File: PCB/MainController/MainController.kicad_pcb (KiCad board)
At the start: 2 copper layers, 124 x 48 mm, 58 parts, among them J1 5V, J10 Jack-DC, J11 MH, J12 MH, J2 PGM, J3 SERIAL, J4 I2C, J5 IO, J6 PWR, J7 MH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

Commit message: opening mplab
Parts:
- added J13: PIC_IO, Pin_Headers:Pin_Header_Straight_1x05_Pitch2.54mm, F.Cu at (131.0, 62.5)
- moved D5 5.41 mm to (139.0, 71.5)
- moved D6 5.41 mm to (139.0, 69.5)
- moved D7 5.41 mm to (139.0, 67.5)
- moved R14 5.41 mm to (134.0, 67.5)
- moved R15 5.41 mm to (134.0, 69.5)
- moved R16 5.41 mm to (134.0, 71.5)
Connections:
- net Net-(R14-Pad2) renamed /RA0
- net Net-(R15-Pad2) renamed /RA1
- net Net-(R16-Pad2) renamed /RB0
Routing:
- net /RB0: track 11.2 -> 32.2 mm
- net /RA1: track 9.11 -> 26.7 mm, vias 0 -> 2
- net /RA0: track 7.02 -> 21.3 mm, vias 0 -> 2
- net GND: track 40.7 -> 39.9 mm
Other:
- board text added: "3.3V"
- board text added: "5V"
- board text added: "Gnd"
- board text added: "RA0"
- board text added: "RA1"
- board text added: "RB0"

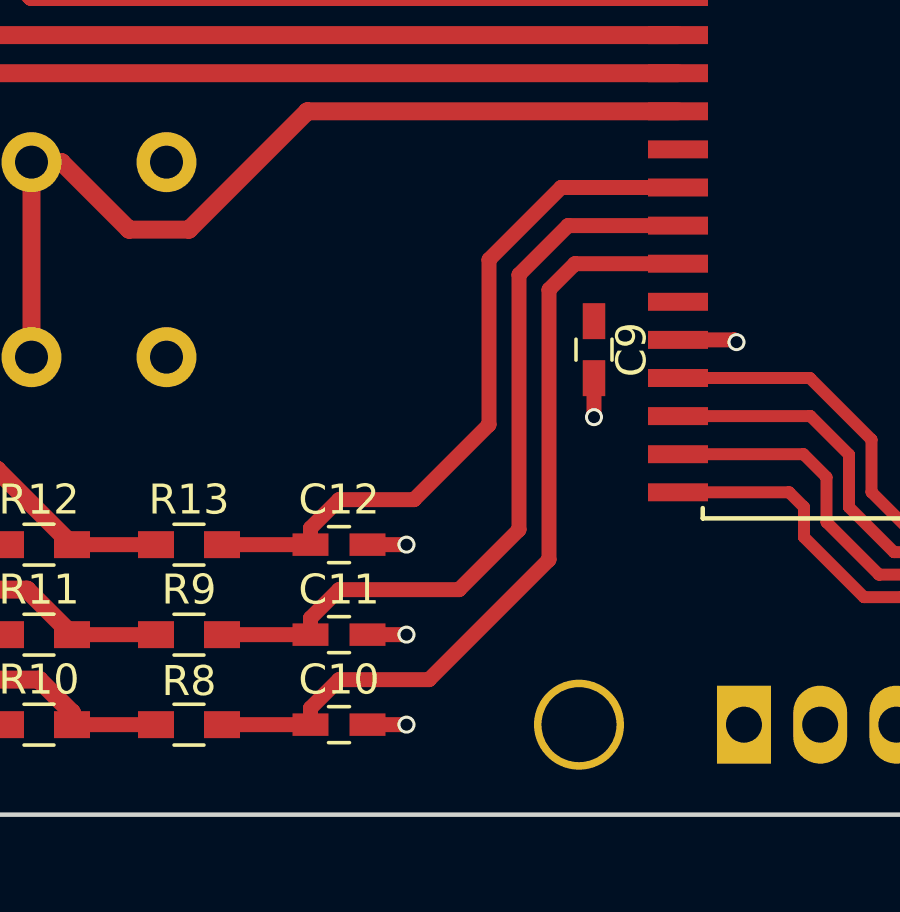
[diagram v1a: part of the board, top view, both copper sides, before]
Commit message: updated pcb for MPC23S power supply error
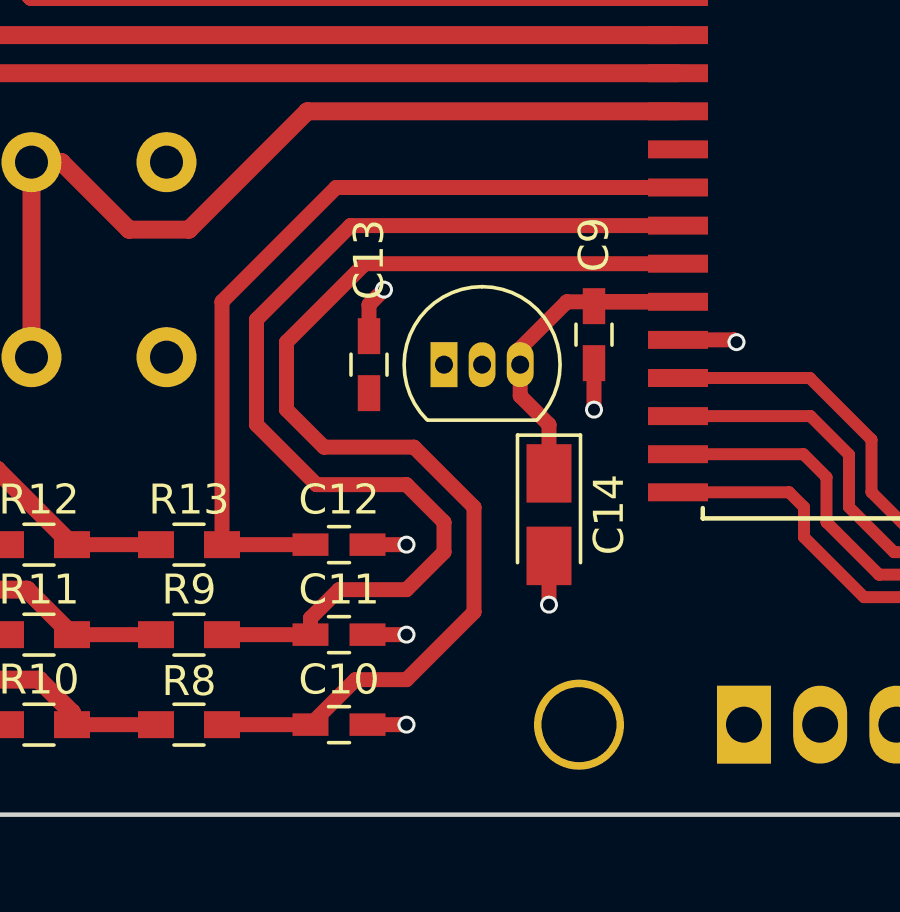
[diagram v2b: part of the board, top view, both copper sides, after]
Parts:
- added C13: 100n, Capacitors_SMD:C_0603_HandSoldering, F.Cu at (69.0, 69.0)
- added C14: 1µ, Capacitors_Tantalum_SMD:CP_Tantalum_Case-A_EIA-3216-18_Reflow, F.Cu at (75.0, 74.0)
- added U5: MCP1700, TO_SOT_Packages_THT:TO-92_Inline_Narrow_Oval, F.Cu at (71.5, 69.0)
- moved C9 0.50 mm to (76.5, 68.0)
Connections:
- C9 pad 1: +5V -> Net-(C14-Pad1)
- U4 pad 9: +5V -> Net-(C14-Pad1)
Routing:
- net Net-(C14-Pad1): track 0.00 -> 13.3 mm
- net /ROT_R1: track 27.2 -> 37.5 mm
- net /ROT_R2: track 26.1 -> 36.3 mm
- net /ROT_B1: track 23.7 -> 27.8 mm
- net GND: track 39.9 -> 43.6 mm, vias 26 -> 28
